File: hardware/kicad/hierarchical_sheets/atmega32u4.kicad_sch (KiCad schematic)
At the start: 39 parts, among them J6 0475900001, J7 TC2030, U11 ATmega32U4-A, Y1 16MHz

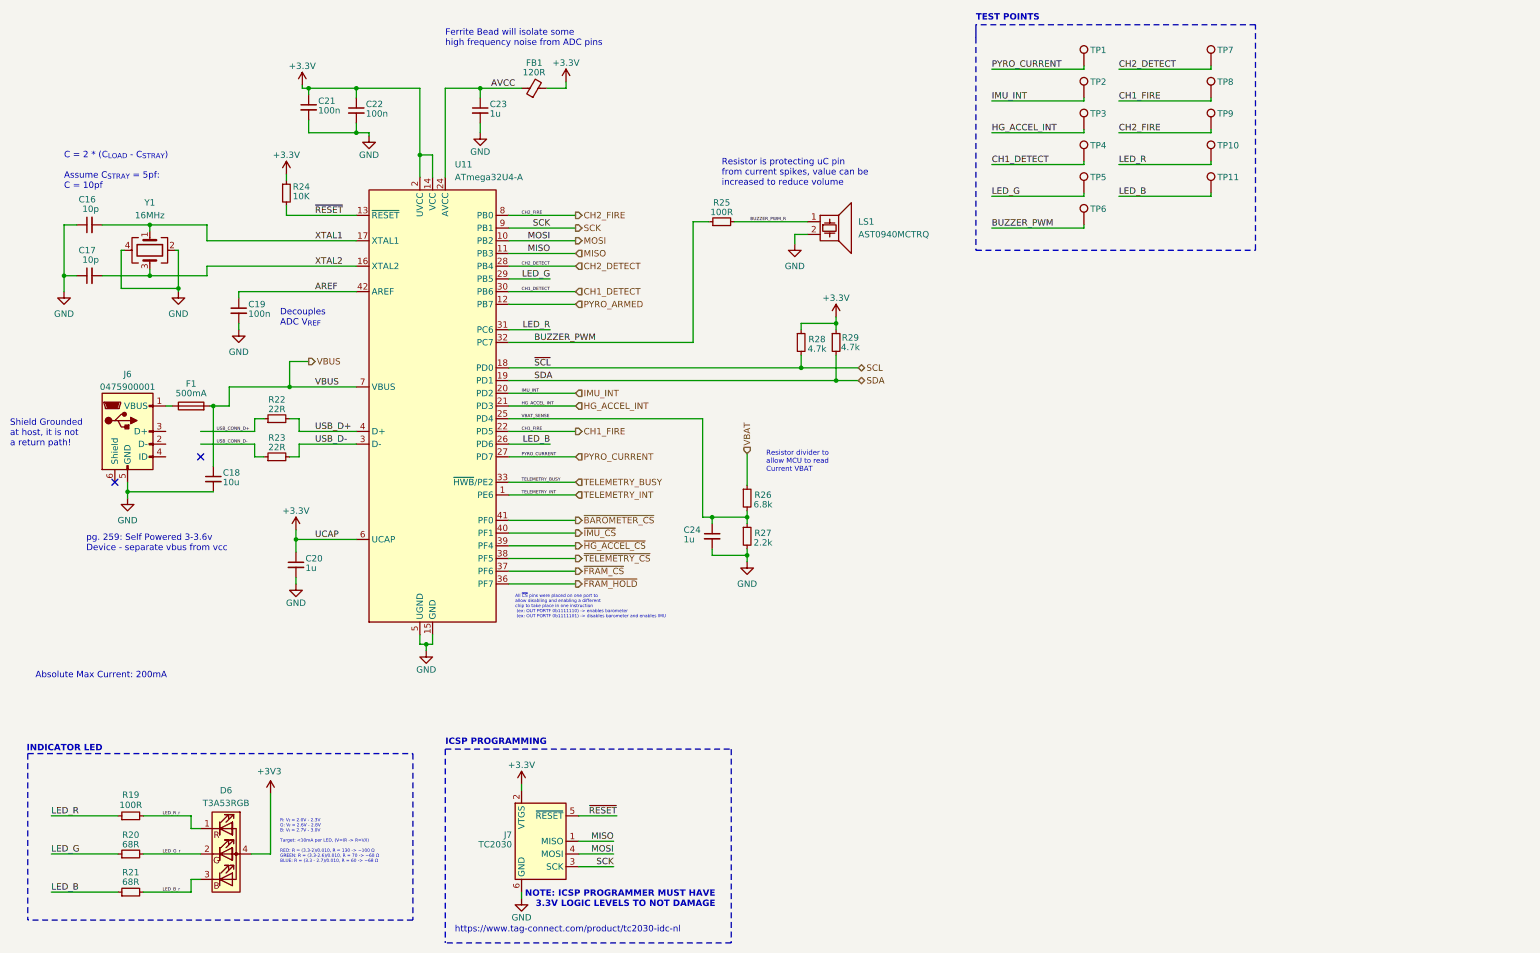
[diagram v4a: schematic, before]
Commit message: all footprints have been fixed
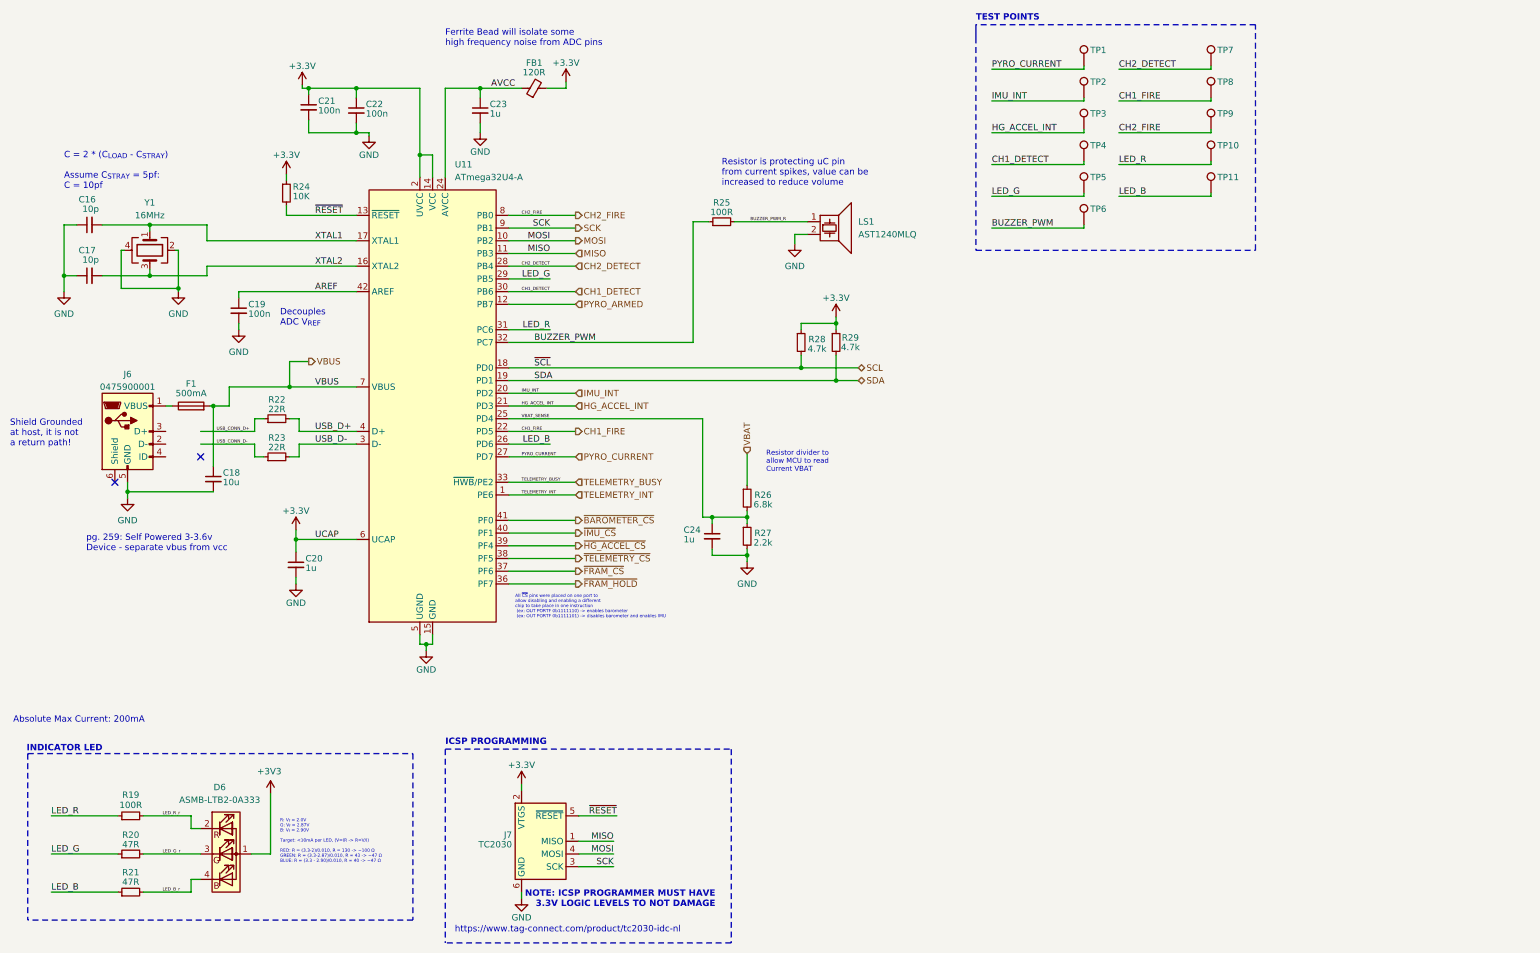
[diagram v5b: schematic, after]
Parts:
- D6: value T3A53RGB -> ASMB-LTB2-0A333; footprint (none) -> ASMB-LTB2:ASMB-LTB2; Digikey https://www.digikey.com/en/products/detail/harvatek-corpora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 -> https://www.digikey.com/en/products/detail/broadcom-limited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
- LS1: value AST0940MCTRQ -> AST1240MLQ; footprint (none) -> Buzzer_Beeper:Buzzer_Mallory_AST1240MLQ; Digikey https://www.digikey.com/en/products/detail/mallory-sonalert-products-inc/AST0940MCTRQ/11567567 -> https://www.digikey.com/en/products/detail/mallory-sonalert-products-inc/AST1240MLQ/5181382
- R20, R21: value 68R -> 47R
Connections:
- net +3V3: now also D6.1 (A); no longer D6.4 (A)
- net LED_B_r: now also D6.4 (BK); no longer D6.3 (BK)
- net LED_G_r: now also D6.3 (GK); no longer D6.2 (GK)
- net LED_R_r: now also D6.2 (RK); no longer D6.1 (RK)
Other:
- note added: "R: V_{f} = 2.0V G: V_{f} = 2.87V B: V_{f} = 2.90V Target: <10mA per LED, (V=IR -> R=V/I) RED: R = (3.3-2)/0.010, R = 130 -> ~100 Ω GREEN: R = (3.3-2.87)/0.010, R = 43 -> ~47 Ω BLUE: R = (3.3 - 2.90)/0.010, R = 40 -> ~47 Ω"
- note removed: "R: V_{f} = 2.0V - 2.3V G: V_{f} = 2.6V - 2.8V B: V_{f} = 2.7V - 3.0V Target: <10mA per LED, (V=IR -> R=V/I) RED: R = (3.3-2)/0.010, R = 130 -> ~100 Ω GREEN: R = (3.3-2.6)/0.010, R = 70 -> ~68 Ω BLUE: R = (3.3 - 2.7)/0.010, R = 60 -> ~68 Ω"
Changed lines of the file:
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@@
     (effects (font (size 1 1)) (justify left bottom))
   )
-  (text "Absolute Max Current: 200mA" (at 17.78 150.495 0)
+  (text "Absolute Max Current: 200mA" (at 13.335 159.385 0)
     (effects (font (size 1.27 1.27)) (justify left bottom))
   )
@@
     (effects (font (size 1.27 1.27) (thickness 0.254) bold) (justify left bottom))
   )
-  (text "R: V_{f} = 2.0V - 2.3V\nG: V_{f} = 2.6V - 2.8V\nB: V_{f} = 2.7V - 3.0V\n\nTarget: <10mA per LED, (V=IR -> R=V/I)\n\nRED: R = (3.3-2)/0.010, R = 130 -> ~100 Ω\nGREEN: R = (3.3-2.6)/0.010, R = 70 -> ~68 Ω\nBLUE: R = (3.3 - 2.7)/0.010, R = 60 -> ~68 Ω"
+  (text "R: V_{f} = 2.0V\nG: V_{f} = 2.87V\nB: V_{f} = 2.90V\n\nTarget: <10mA per LED, (V=IR -> R=V/I)\n\nRED: R = (3.3-2)/0.010, R = 130 -> ~100 Ω\nGREEN: R = (3.3-2.87)/0.010, R = 43 -> ~47 Ω\nBLUE: R = (3.3 - 2.90)/0.010, R = 40 -> ~47 Ω"
     (at 66.675 187.325 0)
     (effects (font (size 0.63 0.63)) (justify left bottom))
@@
       (effects (font (size 1.27 1.27)))
     )
-    (property "Value" "68R" (at 36.83 183.515 90)
+    (property "Value" "47R" (at 36.83 183.515 90)
       (effects (font (size 1.27 1.27)))
     )
@@
   )
   (symbol (lib_id "Device:LED_RGBA") (at 55.88 185.42 0) (unit 1)
-    (in_bom yes) (on_board yes) (dnp no) (fields_autoplaced)
-    (property "Reference" "D6" (at 55.88 172.72 0)
-      (effects (font (size 1.27 1.27)))
-    )
-    (property "Value" "T3A53RGB" (at 55.88 175.26 0)
-      (effects (font (size 1.27 1.27)))
-    )
-    (property "Footprint" "" (at 55.88 186.69 0)
-      (effects (font (size 1.27 1.27)) hide)
-    )
-    (property "Datasheet" "https://mm.digikey.com/Volume0/opasdata/d220001/medias/docus/4890/T3A53RGB-12C610111U1930.pdf" (at 55.88 186.69 0)
-      (effects (font (size 1.27 1.27)) hide)
-    )
-    (property "Digikey" "https://www.digikey.com/en/products/detail/harvatek-corporation/T3A53RGB-12C610111U1930/18997146" (at 55.88 185.42 0)
+    (in_bom yes) (on_board yes) (dnp no)
+    (property "Reference" "D6" (at 54.61 172.085 0)
+      (effects (font (size 1.27 1.27)))
+    )
+    (property "Value" "ASMB-LTB2-0A333" (at 54.61 174.625 0)
+      (effects (font (size 1.27 1.27)))
+    )
+    (property "Footprint" "ASMB-LTB2:ASMB-LTB2" (at 55.88 195.58 0)
+      (effects (font (size 1.27 1.27)) hide)
+    )
+    (property "Datasheet" "https://docs.broadcom.com/docs/ASMB-LTB2-0A333-2121-Tricolor-PLCC-4-LED-DS" (at 58.42 196.85 0)
+      (effects (font (size 1.27 1.27)) hide)
+    )
+    (property "Digikey" "https://www.digikey.com/en/products/detail/broadcom-limited/ASMB-LTB2-0A333/9740374" (at 58.42 195.58 0)
       (effects (font (size 1.27 1.27)) hide)
     )
@@
       (effects (font (size 1.27 1.27)) (justify left))
     )
-    (property "Value" "AST0940MCTRQ" (at 182.245 61.595 0)
-      (effects (font (size 1.27 1.27)) (justify left))
-    )
-    (property "Footprint" "" (at 176.276 60.325 0)
-      (effects (font (size 1.27 1.27)) hide)
-    )
-    (property "Datasheet" "https://www.mouser.com/datasheet/2/252/AST0940MCTRQ-3220277.pdf" (at 176.276 60.325 0)
-      (effects (font (size 1.27 1.27)) hide)
-    )
-    (property "Digikey" "https://www.digikey.com/en/products/detail/mallory-sonalert-products-inc/AST0940MCTRQ/11567567" (at 177.165 59.055 0)
+    (property "Value" "AST1240MLQ" (at 182.245 61.595 0)
+      (effects (font (size 1.27 1.27)) (justify left))
+    )
+    (property "Footprint" "Buzzer_Beeper:Buzzer_Mallory_AST1240MLQ" (at 176.276 60.325 0)
+      (effects (font (size 1.27 1.27)) hide)
+    )
+    (property "Datasheet" "https://www.mspindy.com/spec-sheets/AST1240MLQ.pdf" (at 176.276 60.325 0)
+      (effects (font (size 1.27 1.27)) hide)
+    )
+    (property "Digikey" "https://www.digikey.com/en/products/detail/mallory-sonalert-products-inc/AST1240MLQ/5181382" (at 177.165 59.055 0)
       (effects (font (size 1.27 1.27)) hide)
     )
@@
       (effects (font (size 1.27 1.27)))
     )
-    (property "Value" "68R" (at 36.83 191.008 90)
-      (effects (font (size 1.27 1.27)))
-    )
+    (property "Value" "47R" (at 36.83 191.008 90)
+      (effects (font (size 1.27 1.27)))
+    )

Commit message: formatting
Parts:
- renumbered F1 to F3, U11 to U12

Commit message: formatting / exported pdf
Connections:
- net USB_CONN_D+: now also J6.3 (D+)
- net USB_CONN_D-: now also J6.2 (D-)
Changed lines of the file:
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@@
   )
   (no_connect (at 33.655 111.125))
-  (no_connect (at 50.8 106.045))
+  (no_connect (at 43.815 106.045))
   (wire (pts (xy 208.915 60.325) (xy 227.33 60.325))
     (stroke (width 0) (type default))
@@
     (stroke (width 0) (type default))
   )
-  (wire (pts (xy 50.8 100.965) (xy 61.595 100.965))
+  (wire (pts (xy 43.815 100.965) (xy 61.595 100.965))
     (stroke (width 0) (type default))
   )
@@
     (stroke (width 0) (type default))
   )
-  (wire (pts (xy 50.8 103.505) (xy 61.595 103.505))
+  (wire (pts (xy 43.815 103.505) (xy 61.595 103.505))
     (stroke (width 0) (type default))
   )
@@
     (effects (font (size 1.27 1.27)) (justify left bottom))
   )
-  (label "USB_CONN_D+" (at 53.975 100.965 0) (fields_autoplaced)
+  (label "USB_CONN_D+" (at 45.085 100.965 0) (fields_autoplaced)
     (effects (font (size 0.63 0.63)) (justify left bottom))
   )
@@
     (effects (font (size 1.27 1.27)) (justify right bottom))
   )
-  (label "USB_CONN_D-" (at 53.975 103.505 0) (fields_autoplaced)
-    (effects (font (size 0.63 0.63)) (justify left bottom))
-  )
+  (label "USB_CONN_D-" (at 45.085 103.505 0) (fields_autoplaced)
+    (effects (font (size 0.63 0.63)) (justify left bottom))
+  )

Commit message: sync
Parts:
- added C26: 100n, Resistor_SMD:R_0603_1608Metric, symbol Device:C_Small
- added C27: 1u, Resistor_SMD:R_0603_1608Metric, symbol Device:C_Small
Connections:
- net +3V3 is gone; now on net +3.3V: D6.1 (A)
- net +3.3V: now also C26.1
- net AVCC: now also C27.1
- net GND: now also C26.2, C27.2
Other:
- moved on the sheet: FB1
